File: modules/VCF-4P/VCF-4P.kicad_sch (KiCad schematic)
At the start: 40 parts, among them U1 SSI2140, U2 TL074

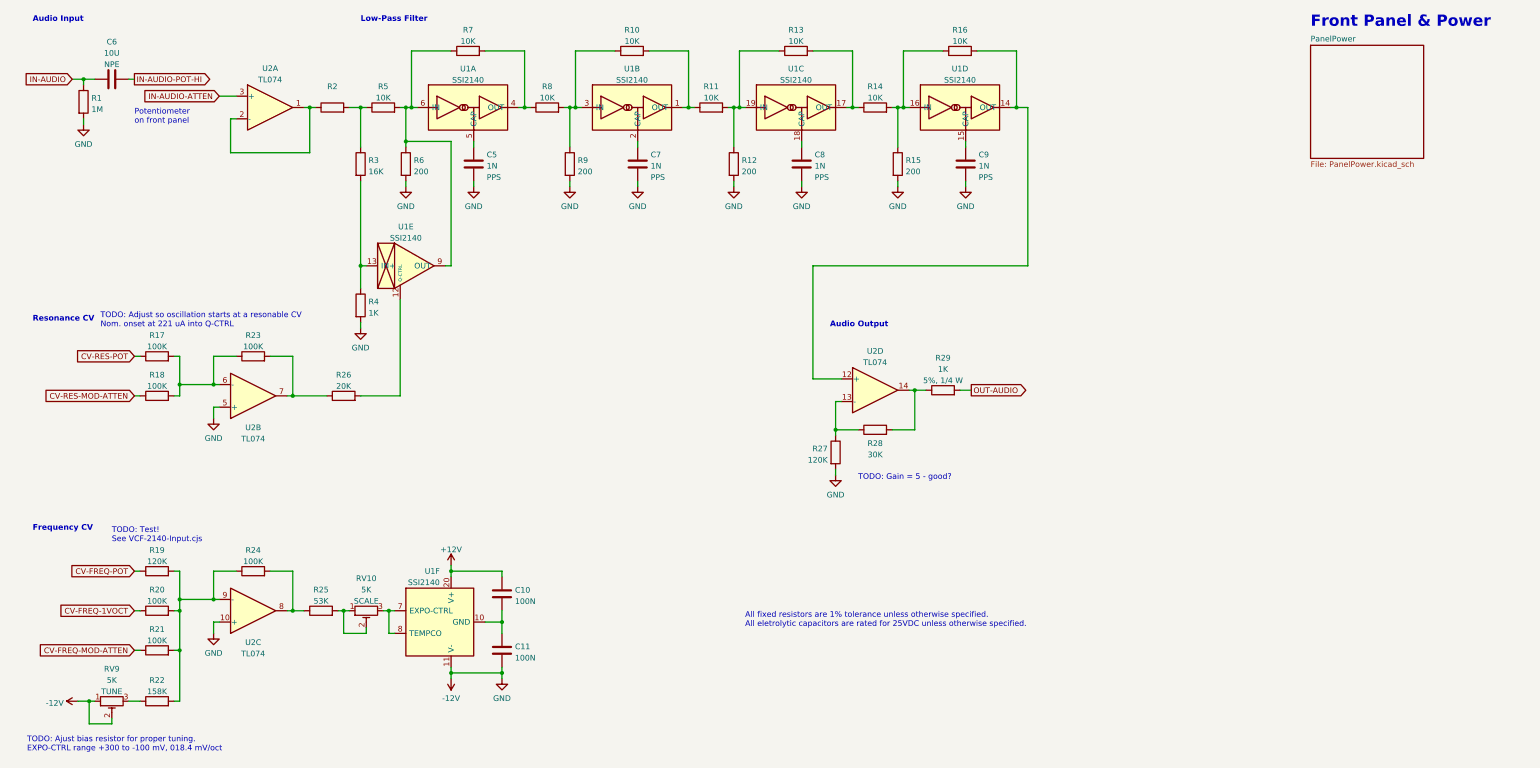
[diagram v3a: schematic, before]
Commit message: VCF-4P: Schematic tweaks
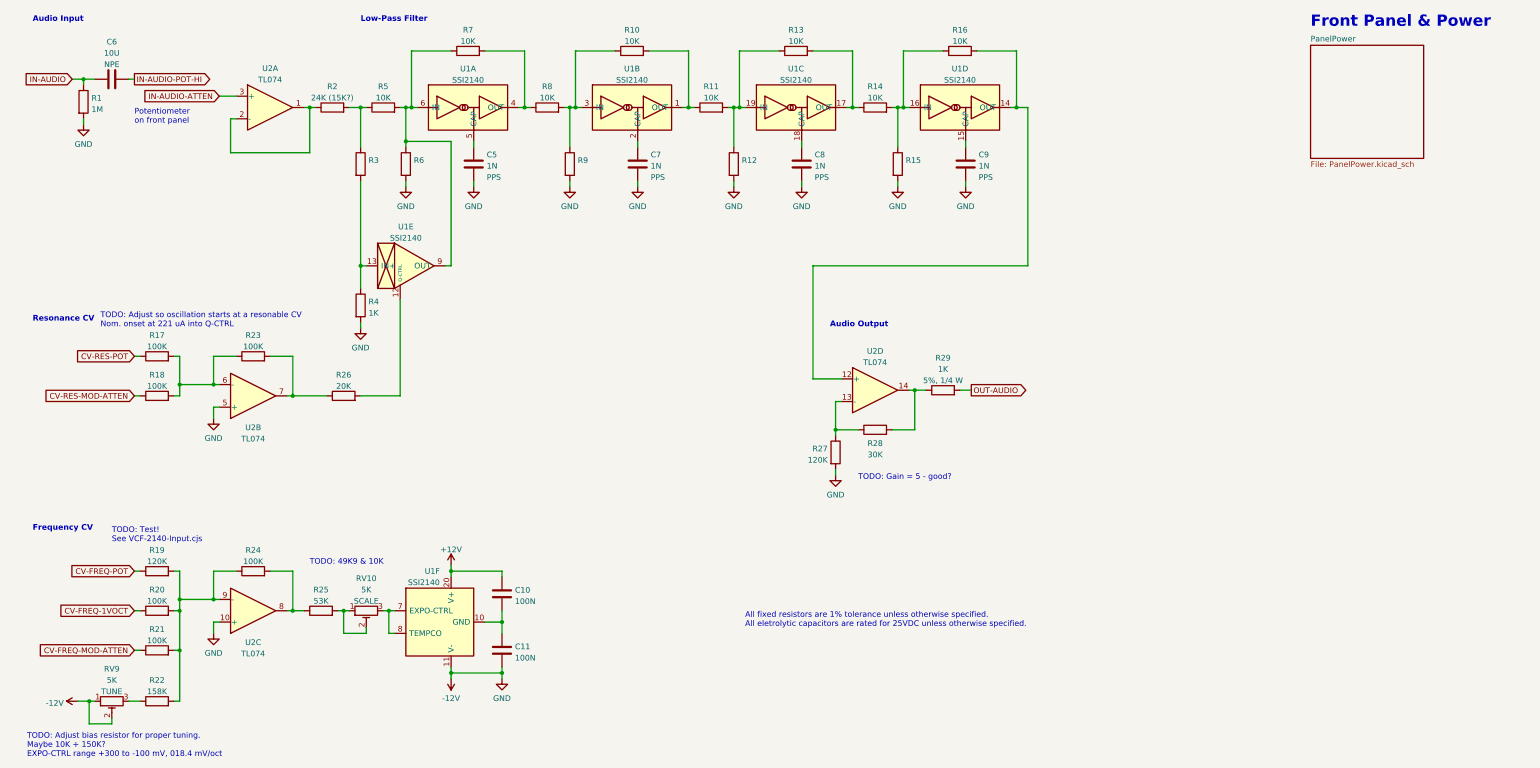
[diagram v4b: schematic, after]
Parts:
- R12, R15, R9: value 200 -> (none)
- R2: value (none) -> 24K (15K?); footprint (none) -> -lmp-misc:R_Axial_DIN0207_L6.3mm_D2.5mm_P7.62mm_Horizontal
- R3: value 16K -> (none); footprint -lmp-misc:R_Axial_DIN0207_L6.3mm_D2.5mm_P7.62mm_Horizontal -> (none); DistributorPartLink https://www.mouser.ca/c/?m=YAGEO&power+rating=166+mW+(1%2f6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 -> https://www.mouser.ca/ProductDetail/YAGEO/MFR-12FTF52-16K?q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; DistributorPartNum 603-MFR-12* -> 603-MFR-12FTF52-16K; ManufacturerPartNum MFR-12* -> MFR-12FTF52-16K
- R6: value 200 -> (none); footprint -lmp-misc:R_Axial_DIN0207_L6.3mm_D2.5mm_P7.62mm_Horizontal -> (none)
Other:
- note added: "TODO: 49K9 & 10K"
- note added: "TODO: Adjust bias resistor for proper tuning. Maybe 10K + 150K? EXPO-CTRL range +300 to -100 mV, 018.4 mV/oct"
- note removed: "TODO: Ajust bias resistor for proper tuning. EXPO-CTRL range +300 to -100 mV, 018.4 mV/oct"
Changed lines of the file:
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@@
+    (effects (font (size 1.27 1.27)) (justify left bottom))
+  )
+  (text "TODO: 49K9 & 10K" (at 80.01 142.24 0)
     (effects (font (size 1.27 1.27)) (justify left bottom))
   )
@@
     (effects (font (size 1.27 1.27)) (justify left bottom))
   )
-  (text "TODO: Ajust bias resistor for proper tuning.\nEXPO-CTRL range +300 to -100 mV, 018.4 mV/oct"
-    (at 16.51 184.15 0)
+  (text "TODO: Adjust bias resistor for proper tuning.\nMaybe 10K + 150K?\nEXPO-CTRL range +300 to -100 mV, 018.4 mV/oct"
+    (at 16.51 185.42 0)
     (effects (font (size 1.27 1.27)) (justify left bottom))
   )
@@
       (effects (font (size 1.27 1.27)) (justify left))
     )
-    (property "Value" "200" (id 1) (at 177.038 53.7722 0)
+    (property "Value" "" (id 1) (at 177.038 53.7722 0)
       (effects (font (size 1.27 1.27)) (justify left))
     )
@@
       (effects (font (size 1.27 1.27)) (justify left))
     )
-    (property "Value" "16K" (id 1) (at 93.218 53.7722 0)
-      (effects (font (size 1.27 1.27)) (justify left))
-    )
-    (property "Footprint" "-lmp-misc:R_Axial_DIN0207_L6.3mm_D2.5mm_P7.62mm_Horizontal" (id 2) (at 89.662 52.07 90)
+    (property "Value" "" (id 1) (at 93.218 53.7722 0)
+      (effects (font (size 1.27 1.27)) (justify left))
+    )
+    (property "Footprint" "" (id 2) (at 89.662 52.07 90)
       (effects (font (size 1.27 1.27)) hide)
     )
@@
       (effects (font (size 1.27 1.27)) hide)
     )
-    (property "ManufacturerPartNum" "MFR-12*" (id 5) (at 91.44 52.07 0)
+    (property "ManufacturerPartNum" "MFR-12FTF52-16K" (id 5) (at 91.44 52.07 0)
       (effects (font (size 1.27 1.27)) hide)
     )
@@
       (effects (font (size 1.27 1.27)) hide)
     )
-    (property "DistributorPartNum" "603-MFR-12*" (id 7) (at 91.44 52.07 0)
-      (effects (font (size 1.27 1.27)) hide)
-    )
-    (property "DistributorPartLink" "https://www.mouser.ca/c/?m=YAGEO&power+rating=166+mW+(1%2f6+W)&tolerance=1+%25&instock=y" (id 8) (at 91.44 52.07 0)
+    (property "DistributorPartNum" "603-MFR-12FTF52-16K" (id 7) (at 91.44 52.07 0)
+      (effects (font (size 1.27 1.27)) hide)
+    )
+    (property "DistributorPartLink" "https://www.mouser.ca/ProductDetail/YAGEO/MFR-12FTF52-16K?qs=oAGoVhmvjhx15wIhq7XW0w%3D%3D" (id 8) (at 91.44 52.07 0)
       (effects (font (size 1.27 1.27)) hide)
     )
@@
       (effects (font (size 1.27 1.27)) (justify left))
     )
-    (property "Value" "200" (id 1) (at 140.208 53.7722 0)
+    (property "Value" "" (id 1) (at 140.208 53.7722 0)
       (effects (font (size 1.27 1.27)) (justify left))
     )
@@
       (effects (font (size 1.27 1.27)) (justify left))
     )
-    (property "Value" "200" (id 1) (at 103.378 53.7722 0)
-      (effects (font (size 1.27 1.27)) (justify left))
-    )
-    (property "Footprint" "-lmp-misc:R_Axial_DIN0207_L6.3mm_D2.5mm_P7.62mm_Horizontal" (id 2) (at 99.822 52.07 90)
+    (property "Value" "" (id 1) (at 103.378 53.7722 0)
+      (effects (font (size 1.27 1.27)) (justify left))
+    )
+    (property "Footprint" "" (id 2) (at 99.822 52.07 90)
       (effects (font (size 1.27 1.27)) hide)
     )
@@
     (in_bom yes) (on_board yes) (fields_autoplaced)
     (property "Reference" "R2" (id 0) (at 85.09 34.6542 90))
-    (property "Value" "" (id 1) (at 85.09 37.1911 90))
-    (property "Footprint" "" (id 2) (at 85.09 41.148 90)
+    (property "Value" "24K (15K?)" (id 1) (at 85.09 37.1911 90))
+    (property "Footprint" "-lmp-misc:R_Axial_DIN0207_L6.3mm_D2.5mm_P7.62mm_Horizontal" (id 2) (at 85.09 41.148 90)
       (effects (font (size 1.27 1.27)) hide)
     )
@@
       (effects (font (size 1.27 1.27)) (justify left))
     )
-    (property "Value" "200" (id 1) (at 213.868 53.7722 0)
+    (property "Value" "" (id 1) (at 213.868 53.7722 0)
       (effects (font (size 1.27 1.27)) (justify left))
     )
@@
     )
     (path "/85e1965d-16ef-4add-83fb-f9a89780cd38"
-      (reference "R6") (unit 1) (value "200") (footprint "-lmp-misc:R_Axial_DIN0207_L6.3mm_D2.5mm_P7.62mm_Horizontal")
+      (reference "R6") (unit 1) (value "200R") (footprint "-lmp-misc:R_Axial_DIN0207_L6.3mm_D2.5mm_P7.62mm_Horizontal")
     )
     (path "/2830192f-4480-43e4-907d-55bfaa371434"
@@
     )
     (path "/84f22fd3-647c-45e6-8f15-96c862aa21ed"
-      (reference "R9") (unit 1) (value "200") (footprint "-lmp-misc:R_Axial_DIN0207_L6.3mm_D2.5mm_P7.62mm_Horizontal")
+      (reference "R9") (unit 1) (value "200R") (footprint "-lmp-misc:R_Axial_DIN0207_L6.3mm_D2.5mm_P7.62mm_Horizontal")
     )
     (path "/eb1d3d7e-6061-4da1-ab3d-065d9c1d2e93"
@@
     )
     (path "/12370933-d5c8-44d4-b1b2-ef3969dc3d1d"
-      (reference "R12") (unit 1) (value "200") (footprint "-lmp-misc:R_Axial_DIN0207_L6.3mm_D2.5mm_P7.62mm_Horizontal")
+      (reference "R12") (unit 1) (value "200R") (footprint "-lmp-misc:R_Axial_DIN0207_L6.3mm_D2.5mm_P7.62mm_Horizontal")
     )
     (path "/f3ba55b2-444b-4e00-a39c-066bc2fb227c"
@@
     )
     (path "/c54226cb-b006-476f-b24b-ee9b04c9c6a7"
-      (reference "R15") (unit 1) (value "200") (footprint "-lmp-misc:R_Axial_DIN0207_L6.3mm_D2.5mm_P7.62mm_Horizontal")
+      (reference "R15") (unit 1) (value "200R") (footprint "-lmp-misc:R_Axial_DIN0207_L6.3mm_D2.5mm_P7.62mm_Horizontal")
     )
     (path "/78b56caf-1fdb-4ca1-a055-cb09468f9ab5"

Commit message: VCF-4P: Correct part numbers for DIP breakout version of SSI2140
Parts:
- C10, C11: value 100N -> (none); footprint -lmp-misc:C_Disc_D5.0mm_W2.5mm_P2.50mm -> (none)
- C5, C7, C8, C9: value 1N -> (none); footprint -lmp-misc:C_Rect_Kemet_L7.2mm_W2.5mm_P5mm -> (none)
- C6: value 10U -> (none); footprint -lmp-misc:C_Radial_D5.0mm_H5.0mm_P2.50mm -> (none)
- R1: value 1M -> (none); footprint -lmp-misc:R_Axial_DIN0207_L6.3mm_D2.5mm_P7.62mm_Horizontal -> (none)
- R10, R11, R13, R14, R16, R5, R7, R8: value 10K -> (none); footprint -lmp-misc:R_Axial_DIN0207_L6.3mm_D2.5mm_P7.62mm_Horizontal -> (none)
- R12, R15, R9: footprint -lmp-misc:R_Axial_DIN0207_L6.3mm_D2.5mm_P7.62mm_Horizontal -> (none)
- R17, R18, R20, R21, R23, R24: value 100K -> (none); footprint -lmp-misc:R_Axial_DIN0207_L6.3mm_D2.5mm_P7.62mm_Horizontal -> (none)
- R19, R27: value 120K -> (none); footprint -lmp-misc:R_Axial_DIN0207_L6.3mm_D2.5mm_P7.62mm_Horizontal -> (none)
- R2: value 24K (15K?) -> (none); footprint -lmp-misc:R_Axial_DIN0207_L6.3mm_D2.5mm_P7.62mm_Horizontal -> (none)
- R22: value 158K -> (none); footprint -lmp-misc:R_Axial_DIN0207_L6.3mm_D2.5mm_P7.62mm_Horizontal -> (none)
- R25: value 53K -> (none); footprint -lmp-misc:R_Axial_DIN0207_L6.3mm_D2.5mm_P7.62mm_Horizontal -> (none)
- R26: value 20K -> (none); footprint -lmp-misc:R_Axial_DIN0207_L6.3mm_D2.5mm_P7.62mm_Horizontal -> (none)
- R28: value 30K -> (none); footprint -lmp-misc:R_Axial_DIN0207_L6.3mm_D2.5mm_P7.62mm_Horizontal -> (none)
- R29: value 1K -> (none); footprint -lmp-misc:R_Axial_DIN0207_L6.3mm_D2.5mm_P10.16mm_Horizontal -> (none)
- R4: value 1K -> (none); footprint -lmp-misc:R_Axial_DIN0207_L6.3mm_D2.5mm_P7.62mm_Horizontal -> (none)
- RV10, RV9: value 5K -> (none); footprint -lmp-synth:Potentiometer_Bourns_3296W_Vertical -> (none)
- U1: value SSI2140 -> (none); footprint -lmp-breakout:Breakout_DIP-20_W15.24mm -> (none); Distributor2 SynthCube -> Thonk; Distributor3 Thonk -> (none); DistributorPartLink https://www.tubesandmore.com/products/integrated-circuit-ss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 -> https://www.tubesandmore.com/products/integrated-circuit-da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; DistributorPartLink2 https://synthcube.com/cart/ics-and-semiconductors/sound-sem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 -> https://www.thonk.co.uk/shop/sound-semiconductor/; DistributorPartLink3 https://www.thonk.co.uk/shop/sound-semiconductor/ -> (none); DistributorPartNum P-Q-SSI2140 -> P-Q-SSIDAB2140; DistributorPartNum2 ICSMSSI2140 -> SSI2140DAB; DistributorPartNum3 SSI2140 -> (none); ManufacturerPartNum SSI2140 -> DAB2140; Note (none) -> SSI2140 on a DIP breakout board
- U2: value TL074 -> (none); footprint Package_DIP:DIP-14_W7.62mm -> (none)

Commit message: VCF-4P: schematic tweaks
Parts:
- C10, C11: value (none) -> 100N; footprint (none) -> -lmp-misc:C_Disc_D5.0mm_W2.5mm_P2.50mm
- C5, C7, C8, C9: value (none) -> 1N; footprint (none) -> -lmp-misc:C_Rect_Kemet_L7.2mm_W2.5mm_P5mm
- C6: value (none) -> 10U; footprint (none) -> -lmp-misc:C_Radial_D5.0mm_H5.0mm_P2.50mm
- R1: value (none) -> 1M; footprint (none) -> -lmp-misc:R_Axial_DIN0207_L6.3mm_D2.5mm_P7.62mm_Horizontal
- R10, R11, R13, R14, R16, R5, R7, R8: value (none) -> 10K; footprint (none) -> -lmp-misc:R_Axial_DIN0207_L6.3mm_D2.5mm_P7.62mm_Horizontal
- R12, R15, R6, R9: value (none) -> 200R; footprint (none) -> -lmp-misc:R_Axial_DIN0207_L6.3mm_D2.5mm_P7.62mm_Horizontal
- R17, R18, R20, R21, R23, R24: value (none) -> 100K; footprint (none) -> -lmp-misc:R_Axial_DIN0207_L6.3mm_D2.5mm_P7.62mm_Horizontal
- R19, R27: value (none) -> 120K; footprint (none) -> -lmp-misc:R_Axial_DIN0207_L6.3mm_D2.5mm_P7.62mm_Horizontal
- R2: value (none) -> 24K (15K?); footprint (none) -> -lmp-misc:R_Axial_DIN0207_L6.3mm_D2.5mm_P7.62mm_Horizontal
- R22: value (none) -> 158K; footprint (none) -> -lmp-misc:R_Axial_DIN0207_L6.3mm_D2.5mm_P7.62mm_Horizontal
- R25: value (none) -> 53K; footprint (none) -> -lmp-misc:R_Axial_DIN0207_L6.3mm_D2.5mm_P7.62mm_Horizontal
- R26: value (none) -> 20K; footprint (none) -> -lmp-misc:R_Axial_DIN0207_L6.3mm_D2.5mm_P7.62mm_Horizontal
- R28: value (none) -> 30K; footprint (none) -> -lmp-misc:R_Axial_DIN0207_L6.3mm_D2.5mm_P7.62mm_Horizontal
- R29: value (none) -> 1K; footprint (none) -> -lmp-misc:R_Axial_DIN0207_L6.3mm_D2.5mm_P10.16mm_Horizontal
- R3: value (none) -> 16K; footprint (none) -> -lmp-misc:R_Axial_DIN0207_L6.3mm_D2.5mm_P7.62mm_Horizontal
- R4: value (none) -> 1K; footprint (none) -> -lmp-misc:R_Axial_DIN0207_L6.3mm_D2.5mm_P7.62mm_Horizontal
- RV10, RV9: value (none) -> 5K; footprint (none) -> -lmp-synth:Potentiometer_Bourns_3296W_Vertical
- U1: value (none) -> SSI2140; footprint (none) -> -lmp-breakout:Breakout_DIP-20_W15.24mm
- U2: value (none) -> TL074; footprint (none) -> Package_DIP:DIP-14_W7.62mm
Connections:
- net at R16.2, U1.14 (OUT): no longer U2.12 (+)
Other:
- note added: "Feedback VCA"
- note added: "TODO: 49K9 & 10K?"
- note added: "TODO: Adjust for gain & overdrive"
- note removed: "TODO: 49K9 & 10K"
- moved on the sheet: C5, C7, C8, C9, R10, R11, R12, R13, R14, R15, R16, R3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

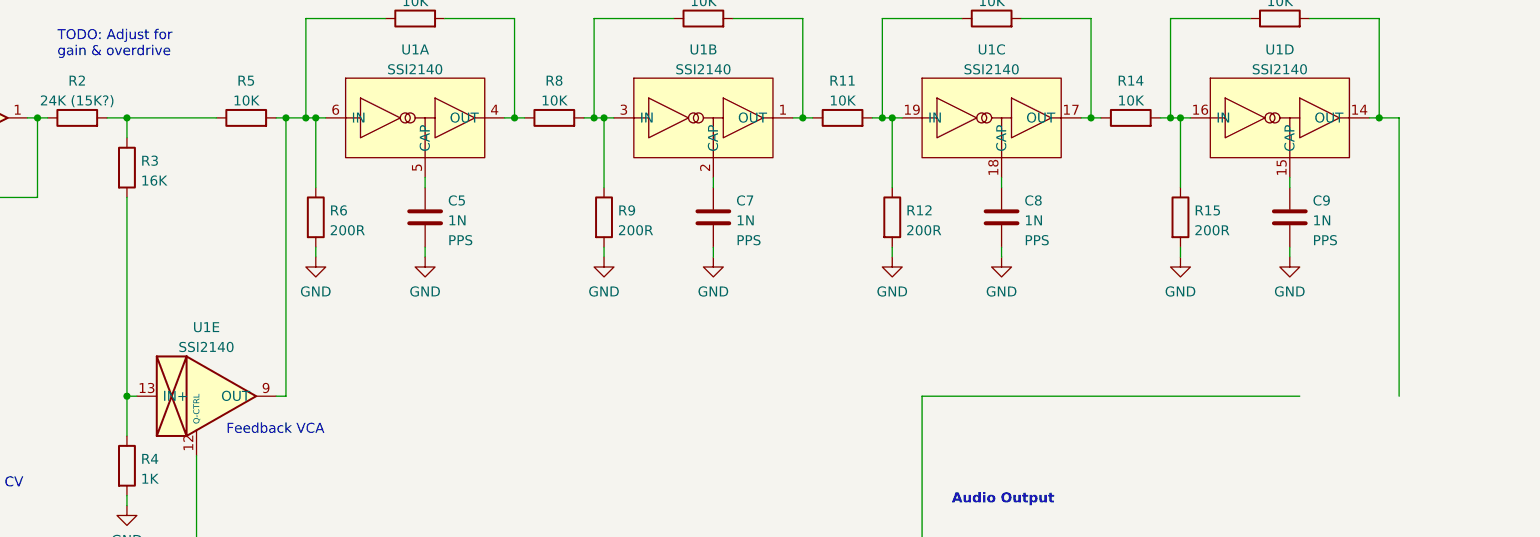
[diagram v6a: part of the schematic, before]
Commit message: VCF-4P: Breadboard prototype, 2-pole version - wip
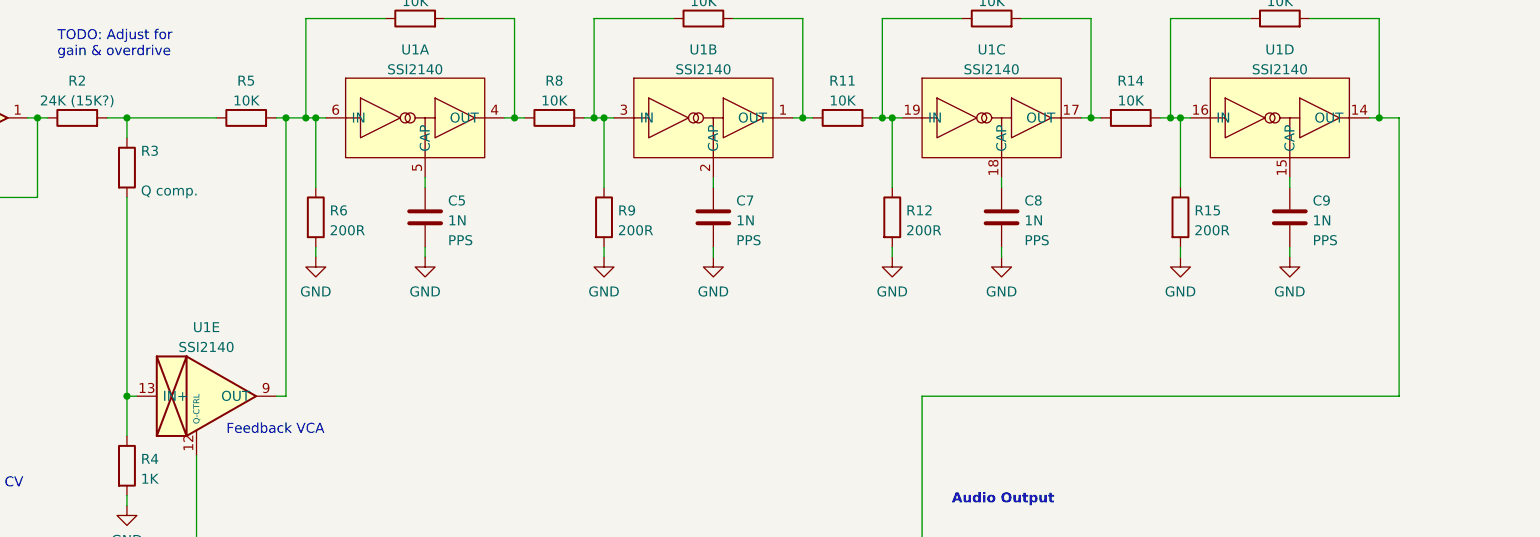
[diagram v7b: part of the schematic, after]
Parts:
- R3: value 16K -> (none); footprint -lmp-misc:R_Axial_DIN0207_L6.3mm_D2.5mm_P7.62mm_Horizontal -> (none); Note (none) -> Q comp.
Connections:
- net at U2.12 (+): now also R16.2, U1.14 (OUT)
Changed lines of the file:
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@@
-    (stroke (width 0) (type default) (color 0 0 0 0))
-  )
-  (wire (pts (xy 241.3 74.93) (xy 193.04 74.93))
     (stroke (width 0) (type default) (color 0 0 0 0))
   )
@@
   )
   (wire (pts (xy 58.42 95.25) (xy 58.42 101.6))
+    (stroke (width 0) (type default) (color 0 0 0 0))
+  )
+  (wire (pts (xy 193.04 74.93) (xy 254 74.93))
     (stroke (width 0) (type default) (color 0 0 0 0))
   )
@@
   (symbol (lib_id "-lmp:R_1%_0W166") (at 91.44 45.72 0) (unit 1)
     (in_bom yes) (on_board yes) (fields_autoplaced)
-    (property "Reference" "R3" (id 0) (at 93.218 44.8853 0)
+    (property "Reference" "R3" (id 0) (at 93.218 43.6169 0)
       (effects (font (size 1.27 1.27)) (justify left))
     )
-    (property "Value" "16K" (id 1) (at 93.218 47.4222 0)
+    (property "Value" "" (id 1) (at 93.218 46.1538 0)
       (effects (font (size 1.27 1.27)) (justify left))
     )
-    (property "Footprint" "-lmp-misc:R_Axial_DIN0207_L6.3mm_D2.5mm_P7.62mm_Horizontal" (id 2) (at 89.662 45.72 90)
+    (property "Footprint" "" (id 2) (at 89.662 45.72 90)
       (effects (font (size 1.27 1.27)) hide)
     )
@@
       (effects (font (size 1.27 1.27)) hide)
     )
-    (pin "1")
+    (property "Note" "Q comp." (id 10) (at 93.218 48.6907 0)
+      (effects (font (size 1.27 1.27)) (justify left))
+    )
+    (pin "1")

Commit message: VCF-4P - wip
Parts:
- R3: value (none) -> 16K; footprint (none) -> -lmp-misc:R_Axial_DIN0207_L6.3mm_D2.5mm_P7.62mm_Horizontal
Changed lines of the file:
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@@
       (effects (font (size 1.27 1.27)) (justify left))
     )
-    (property "Value" "" (id 1) (at 93.218 46.1538 0)
+    (property "Value" "16K" (id 1) (at 93.218 46.1538 0)
       (effects (font (size 1.27 1.27)) (justify left))
     )
-    (property "Footprint" "" (id 2) (at 89.662 45.72 90)
+    (property "Footprint" "-lmp-misc:R_Axial_DIN0207_L6.3mm_D2.5mm_P7.62mm_Horizontal" (id 2) (at 89.662 45.72 90)
       (effects (font (size 1.27 1.27)) hide)
     )
